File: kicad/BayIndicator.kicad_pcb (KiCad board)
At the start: 2 copper layers, 50.8 x 50.8 mm, 3 parts, among them J1 Conn_02x10_Odd_Even, U1 XIAO ESP32C3

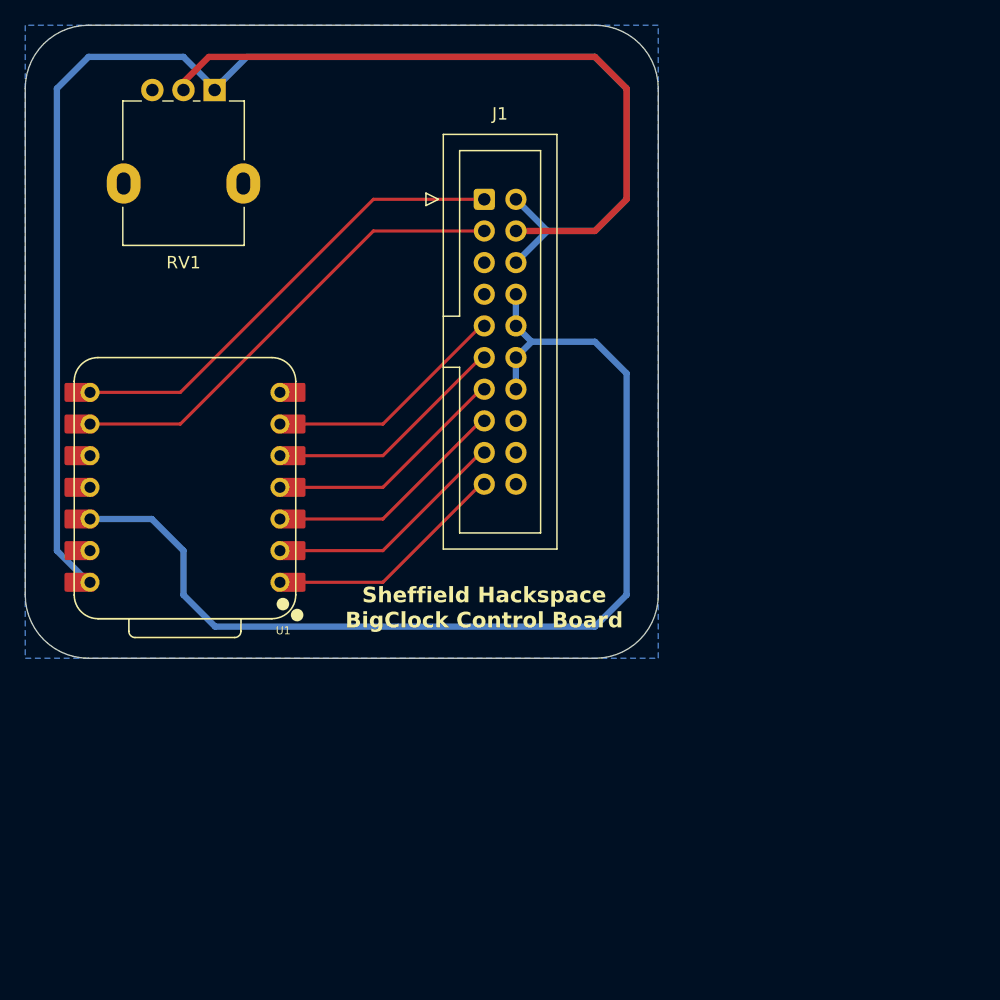
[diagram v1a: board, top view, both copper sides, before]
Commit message: Reconnect to match the actual state
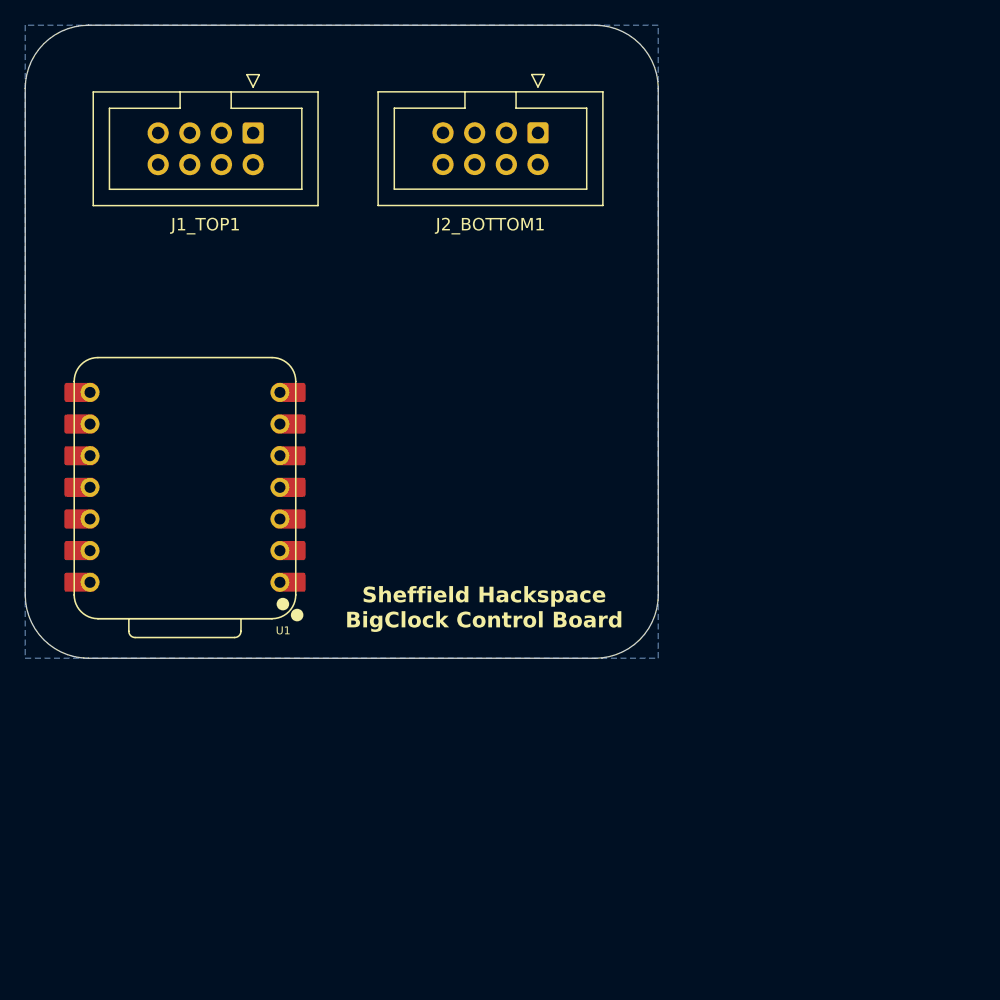
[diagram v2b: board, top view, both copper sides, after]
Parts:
- removed J1: Conn_02x10_Odd_Even, Connector_IDC:IDC-Header_2x10_P2.54mm_Vertical
- removed RV1: R_Potentiometer, kicad-footprints:Potentiometer_Taiwan_Alpha_9mm_Vertical
- added J1_TOP1: Conn_02x04_Odd_Even, Connector_IDC:IDC-Header_2x04_P2.54mm_Vertical, F.Cu at (69.1, 59.4)
- added J2_BOTTOM1: Conn_02x04_Odd_Even, Connector_IDC:IDC-Header_2x04_P2.54mm_Vertical, F.Cu at (91.9, 59.4)
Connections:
- U1 pad 1: /Board 1 DATA CLK -> unconnected-(U1-D0-Pad1)
- U1 pad 10: unconnected-(U1-D9-Pad10) -> /CLK 2
- U1 pad 11: unconnected-(U1-D10-Pad11) -> /LATCH 2
- U1 pad 12: +3V3 -> unconnected-(U1-VCC_3V3-Pad12)
- U1 pad 2: /Board 0 DATA CLK -> unconnected-(U1-D1-Pad2)_1
- U1 pad 3: /Board 1 DATA IN -> unconnected-(U1-D2-Pad3)
- U1 pad 4: /Board 0 DATA IN -> /LATCH 1
- U1 pad 5: /Board 1 LATCH -> /CLK 1
- U1 pad 6: /Board 0 LATCH -> /MOSI 1
- U1 pad 8: /Board 0 CLK -> unconnected-(U1-D7-Pad8)
- U1 pad 9: /Board 1 CLK -> /MOSI 2
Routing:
- net +5V: track 114.2 -> 0.00 mm
- net +3V3: track 84.9 -> 0.00 mm
- net /Contrast: track 56.9 -> 0.00 mm
- net /Board 0 CLK: track 38.3 -> 0.00 mm
- net /Board 1 CLK: track 37.9 -> 0.00 mm
- net /Board 1 DATA IN: track 19.5 -> 0.00 mm
- net /Board 1 LATCH: track 19.5 -> 0.00 mm
- net /Board 0 LATCH: track 19.5 -> 0.00 mm
- net /Board 0 DATA IN: track 19.5 -> 0.00 mm
- net /Board 1 DATA CLK: track 19.5 -> 0.00 mm
- net /Board 0 DATA CLK: track 19.5 -> 0.00 mm

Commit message: Create a PCB for the BayIndicator
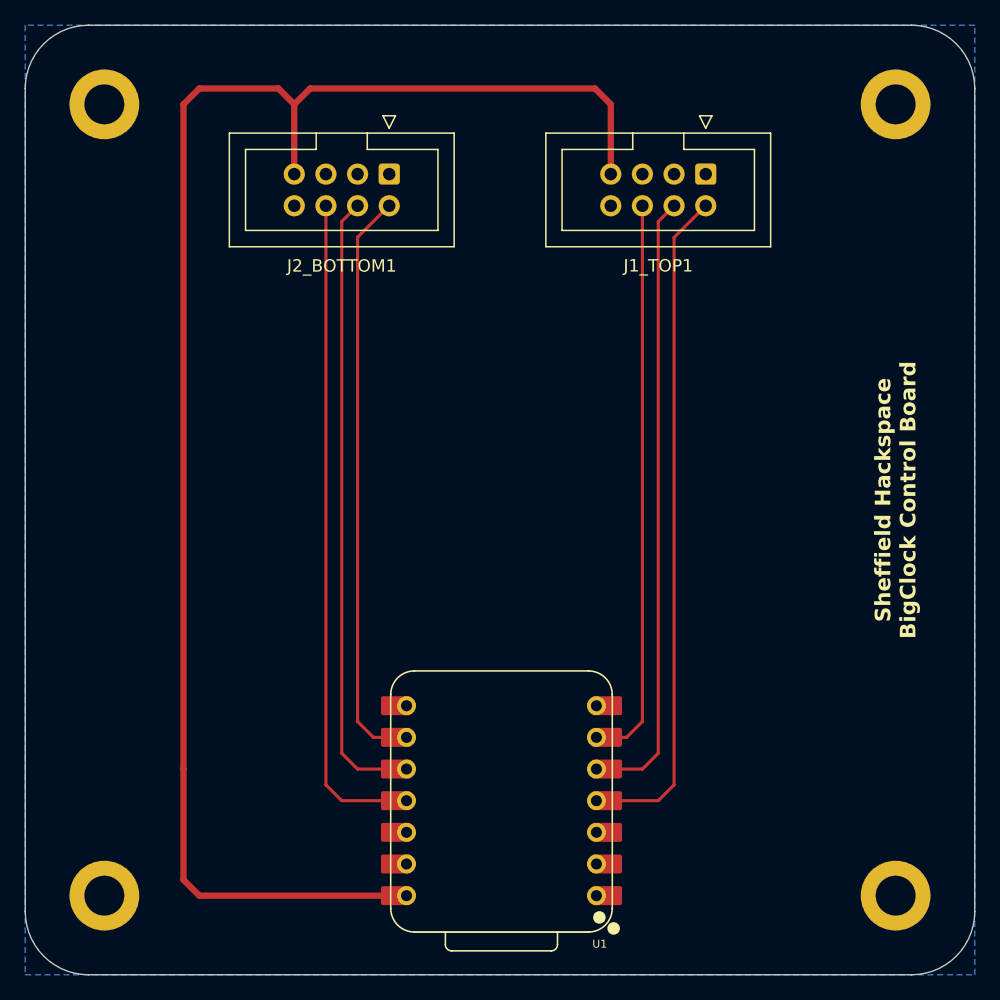
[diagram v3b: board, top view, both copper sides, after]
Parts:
- added REF**: MountingHole_3.2mm_M3_DIN965_Pad, MountingHole:MountingHole_3.2mm_M3_DIN965_Pad, F.Cu at (57.1, 57.1)
- added REF**: MountingHole_3.2mm_M3_DIN965_Pad, MountingHole:MountingHole_3.2mm_M3_DIN965_Pad, F.Cu at (57.1, 120.7)
- added REF**: MountingHole_3.2mm_M3_DIN965_Pad, MountingHole:MountingHole_3.2mm_M3_DIN965_Pad, F.Cu at (120.7, 120.7)
- added REF**: MountingHole_3.2mm_M3_DIN965_Pad, MountingHole:MountingHole_3.2mm_M3_DIN965_Pad, F.Cu at (120.7, 57.1)
- moved J1_TOP1 36.5 mm to (105.4, 62.7)
- moved U1 35.7 mm to (88.9, 113.0)
- moved J2_BOTTOM1 12.4 mm to (80.0, 62.7)
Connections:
- U1 pad 4: /LATCH 1 -> /MOSI 1
- U1 pad 6: /MOSI 1 -> /LATCH 1
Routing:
- net +5V: track 0.00 -> 128.4 mm
- net /MOSI 1: track 0.00 -> 54.4 mm
- net /LATCH 2: track 0.00 -> 53.3 mm
- net /CLK 2: track 0.00 -> 50.1 mm
- net /CLK 1: track 0.00 -> 50.1 mm
- net /MOSI 2: track 0.00 -> 46.8 mm
- net /LATCH 1: track 0.00 -> 45.7 mm
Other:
- board size 50.8 x 50.8 mm -> 76.2 x 76.2 mm

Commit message: PCB design
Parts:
- removed J1_TOP1, J2_BOTTOM1: Conn_02x04_Odd_Even, Connector_IDC:IDC-Header_2x04_P2.54mm_Vertical
- removed the REF** at (120.7, 120.7)
- removed the REF** at (120.7, 57.1)
- added J1: Screw_Terminal_01x02, TerminalBlock:TerminalBlock_MaiXu_MX126-5.0-02P_1x02_P5.00mm, F.Cu at (78.5, 63.5)
- added JBOTTOM1: Conn_02x04_Odd_Even, Connector_IDC:IDC-Header_2x04_P2.54mm_Vertical, F.Cu at (70.1, 92.7)
- added JTOP1: Conn_02x04_Odd_Even, Connector_IDC:IDC-Header_2x04_P2.54mm_Vertical, F.Cu at (82.3, 85.1)
- added REF**: MountingHole_3.2mm_M3_DIN965_Pad, MountingHole:MountingHole_3.2mm_M3_DIN965_Pad, F.Cu at (95.2, 57.1)
- added REF**: MountingHole_3.2mm_M3_DIN965_Pad, MountingHole:MountingHole_3.2mm_M3_DIN965_Pad, F.Cu at (95.2, 120.7)
- moved U1 12.8 mm to (76.1, 113.0)
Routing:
- net +5V: track 128.4 -> 76.7 mm
- net /MOSI 2: track 46.8 -> 20.4 mm
- net /LATCH 1: track 45.7 -> 22.9 mm
- net /CLK 2: track 50.1 -> 28.0 mm
- net /CLK 1: track 50.1 -> 30.5 mm
- net /LATCH 2: track 53.3 -> 35.6 mm
- net /MOSI 1: track 54.4 -> 38.1 mm
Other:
- board size 76.2 x 76.2 mm -> 50.8 x 76.2 mm
- board text added: "Sheffield Hackspace BayIndicator Control Board"
- board text removed: "Sheffield Hackspace BigClock Control Board"
